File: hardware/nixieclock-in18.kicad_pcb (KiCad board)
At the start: 2 copper layers, 79 parts, among them J1 PROG, J2 POWER, Q1 BC848, Q10 MPSA42, Q11 MPSA42, Q12 MPSA42, Q13 MPSA42, Q14 MPSA42, Q15 MPSA42, Q16 MPSA42, Q17 MPSA42, Q18 MPSA42, Q19 MPSA42, Q2 BC858, Q20 MPSA42, Q21 MPSA42, Q3 Si4434, Q4 MPSA42, Q5 MPSA42, Q6 MPSA42, Q7 MPSA42, Q8 MPSA42, Q9 MPSA42, T1 IN18, T2 IN18, T3 IN18, T4 IN18, U1 LM1117-3.3, U2 DS3231M, U3 LM393, U4 ESP32-WROOM-32D

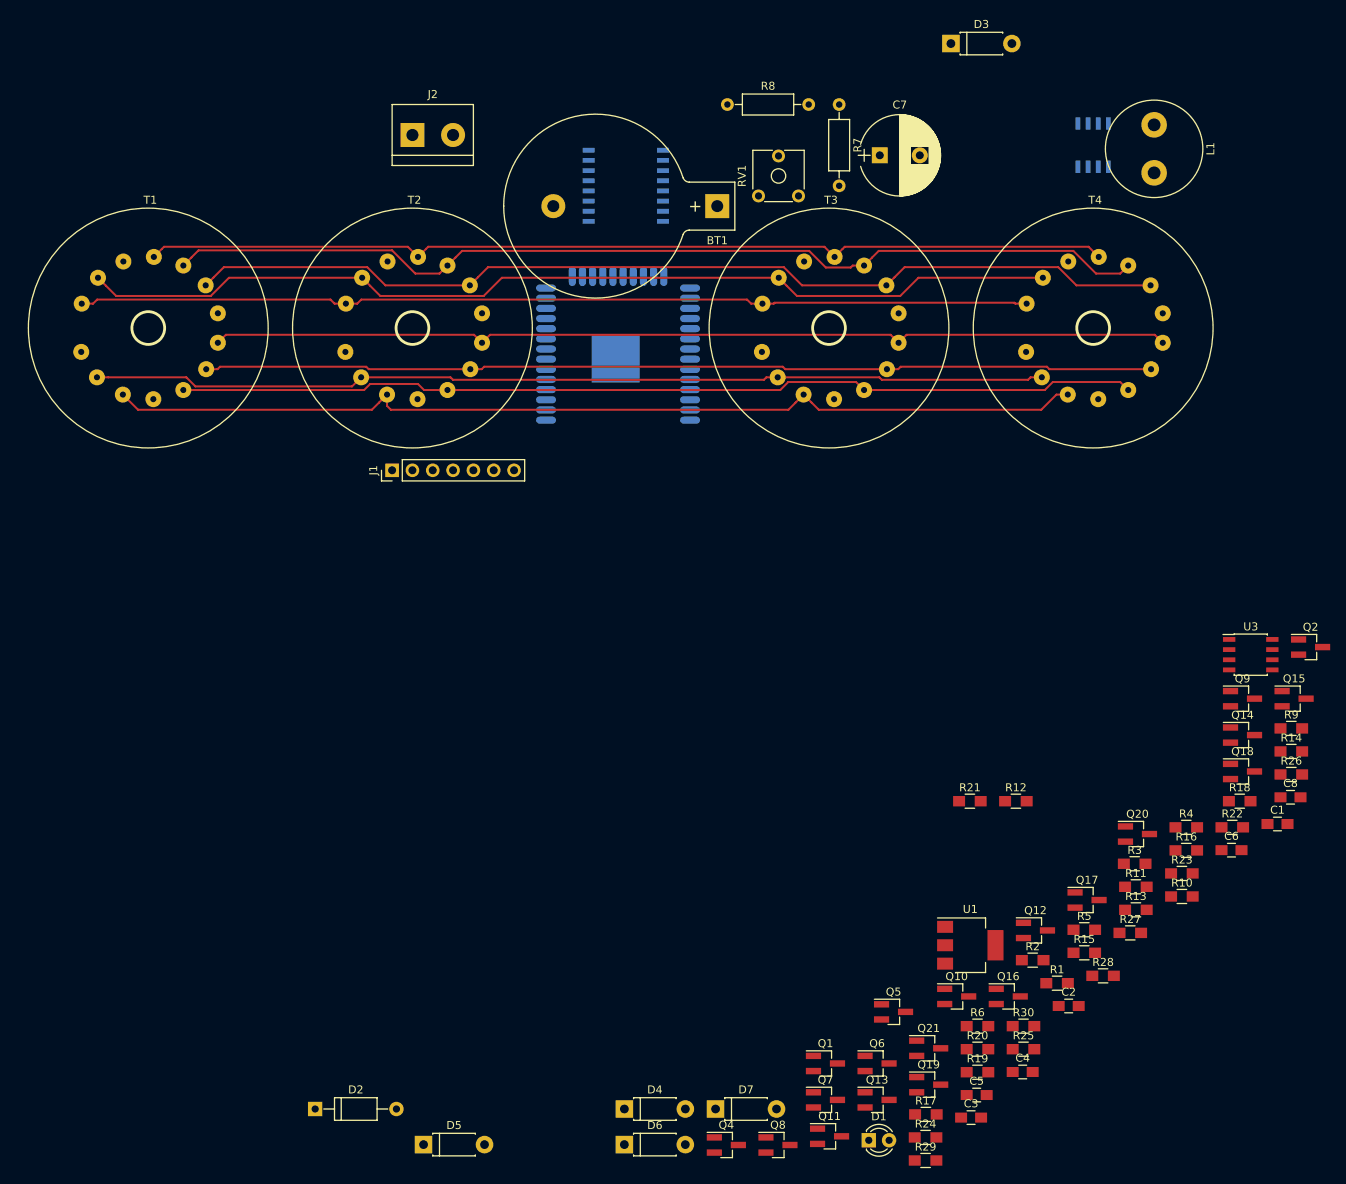
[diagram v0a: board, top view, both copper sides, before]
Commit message: fix mmbta42 pinout
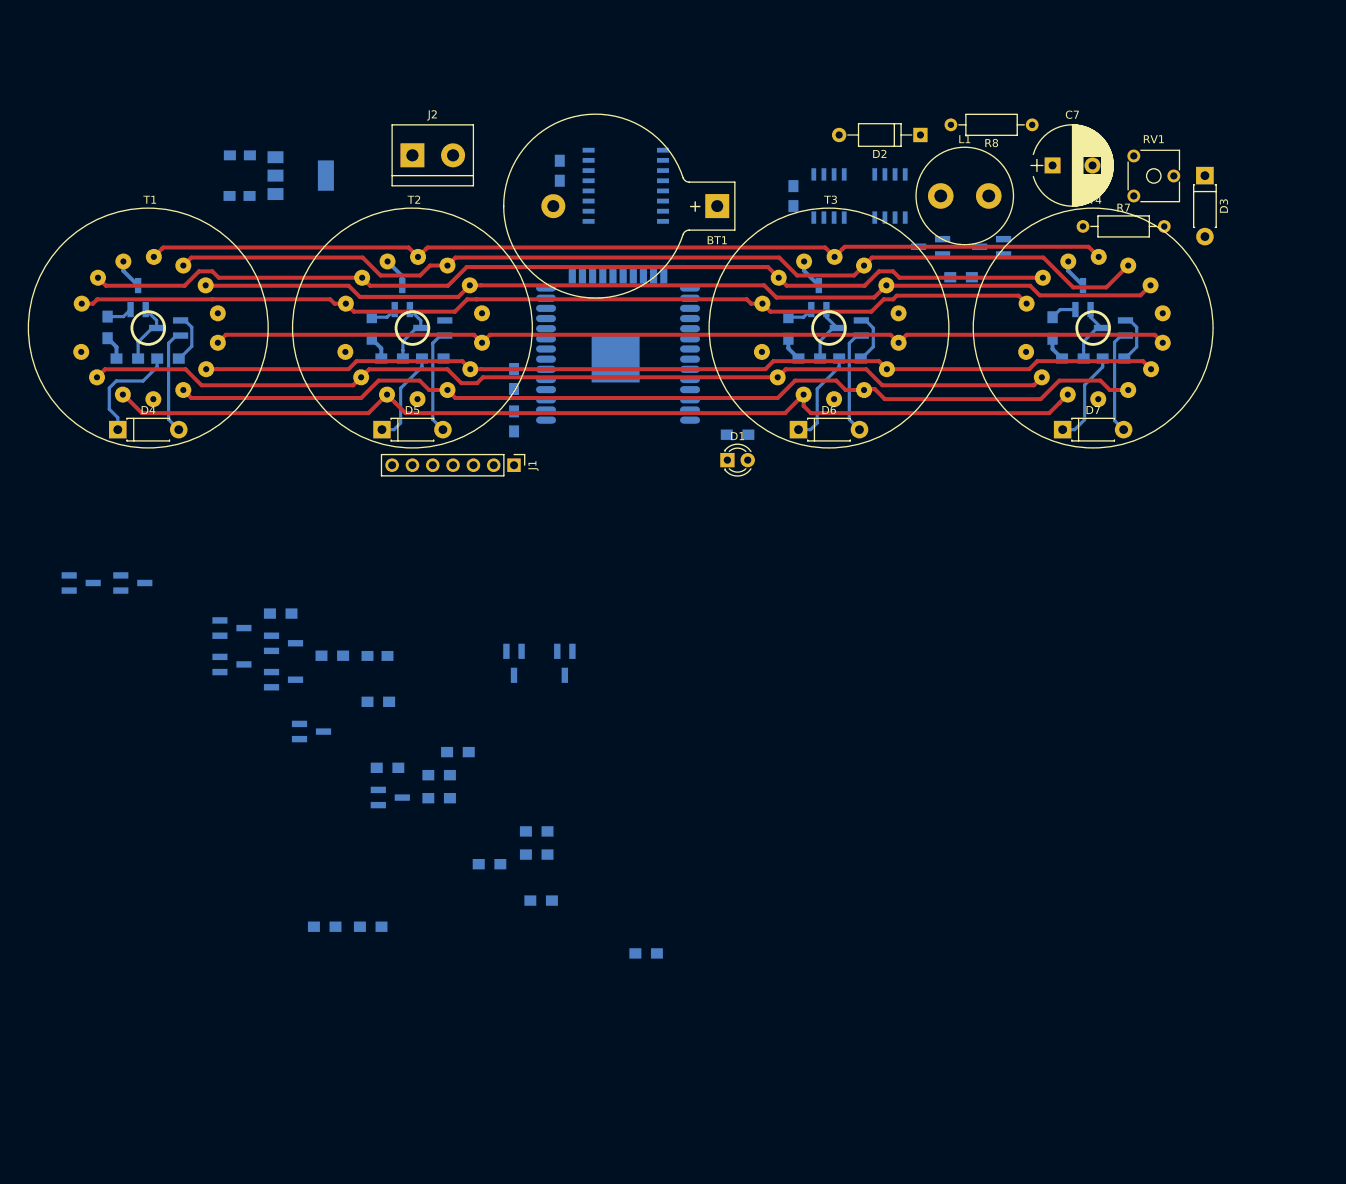
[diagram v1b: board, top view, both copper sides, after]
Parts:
- C1, C2, C3, C4, C5, C6, C8, Q1, Q2, R1, R10, R11, R12, R13, R14, R15, R16, R17, R18, R19, R2, R20, R21, R22, R23, R24, R25, R26, R27, R28, R29, R3, R30, R4, R5, R6, R9, U1, U3: moved to B.Cu
- Q10, Q11, Q12, Q13, Q14, Q15, Q16, Q17, Q18, Q19, Q20, Q21, Q4, Q5, Q6, Q7, Q8, Q9: value MPSA42 -> MMBTA42; moved to B.Cu
- moved C1 154.3 mm to (119.4, 57.1)
- moved R9 147.8 mm to (110.4, 82.5)
- moved R13 147.7 mm to (102.9, 78.7), turned to 270 degrees
- moved C3 147.1 mm to (119.4, 62.2), turned to 180 degrees
- moved D2 143.3 mm to (204.5, 54.6), turned to 180 degrees
- moved R11 142.3 mm to (105.3, 82.5), turned to 180 degrees
- moved Q7 132.1 mm to (106.7, 74.9), turned to 90 degrees
- moved U1 127.5 mm to (127.0, 59.7)
- moved Q5 124.6 mm to (110.5, 78.7), turned to 180 degrees
- moved R18 123.6 mm to (135.9, 78.7), turned to 270 degrees
- moved C2 122.3 mm to (159.4, 59.1), turned to 270 degrees
- moved R14 118.0 mm to (143.5, 82.5)
- moved Q11 117.7 mm to (139.7, 74.9), turned to 90 degrees
- moved R16 116.8 mm to (138.4, 82.5), turned to 180 degrees
- moved C5 114.7 mm to (188.6, 62.2), turned to 270 degrees
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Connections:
- Q10 pad 1: GND -> Net-(Q10-Pad1)
- Q10 pad 2: Net-(Q10-Pad2) -> GND
- Q11 pad 3: Net-(Q11-Pad3) -> /A1
- Q12 pad 1: GND -> Net-(Q12-Pad1)
- Q12 pad 2: Net-(Q12-Pad2) -> GND
- Q13 pad 1: GND -> Net-(Q13-Pad1)
- Q13 pad 2: Net-(Q13-Pad2) -> GND
- Q14 pad 1: GND -> Net-(Q14-Pad1)
- Q14 pad 2: Net-(Q14-Pad2) -> GND
- Q15 pad 1: GND -> Net-(Q15-Pad1)
- Q15 pad 2: Net-(Q15-Pad2) -> GND
- Q16 pad 1: Net-(Q16-Pad1) -> Net-(Q14-Pad3)
- Q16 pad 2: Net-(Q14-Pad3) -> Net-(Q16-Pad2)
- Q16 pad 3: Net-(Q16-Pad3) -> /A2
- Q17 pad 1: GND -> Net-(Q17-Pad1)
- Q17 pad 2: Net-(Q17-Pad2) -> GND
- Q18 pad 1: GND -> Net-(Q18-Pad1)
- Q18 pad 2: Net-(Q18-Pad2) -> GND
- Q19 pad 1: GND -> Net-(Q19-Pad1)
- Q19 pad 2: Net-(Q19-Pad2) -> GND
- Q20 pad 1: Net-(Q20-Pad1) -> Net-(Q18-Pad3)
- Q20 pad 2: Net-(Q18-Pad3) -> Net-(Q20-Pad2)
- Q20 pad 3: Net-(Q20-Pad3) -> /A3
- Q21 pad 1: GND -> Net-(Q21-Pad1)
- Q21 pad 2: Net-(Q21-Pad2) -> GND
- Q4 pad 1: GND -> Net-(Q4-Pad1)
- Q4 pad 2: Net-(Q4-Pad2) -> GND
- Q5 pad 1: GND -> Net-(Q5-Pad1)
- Q5 pad 2: Net-(Q5-Pad2) -> GND
- Q6 pad 1: GND -> Net-(Q6-Pad1)
- Q6 pad 2: Net-(Q6-Pad2) -> GND
- Q7 pad 1: Net-(Q7-Pad1) -> Net-(Q5-Pad3)
- Q7 pad 2: Net-(Q5-Pad3) -> Net-(Q7-Pad2)
- Q7 pad 3: Net-(Q7-Pad3) -> /A0
- Q8 pad 1: GND -> Net-(Q8-Pad1)
- Q8 pad 2: Net-(Q8-Pad2) -> GND
- Q9 pad 1: GND -> Net-(Q9-Pad1)
- Q9 pad 2: Net-(Q9-Pad2) -> GND
- Q9 pad 3: Net-(Q11-Pad2) -> Net-(Q11-Pad1)
- R1 pad 1: LED_SYNC -> (no net)
- R10 pad 1: DIG0 -> (no net)
- R10 pad 2: Net-(Q4-Pad2) -> Net-(Q4-Pad1)
- R12 pad 1: DIG1 -> (no net)
- R12 pad 2: Net-(Q6-Pad2) -> Net-(Q6-Pad1)
- R13 pad 1: Net-(Q7-Pad3) -> Net-(Q7-Pad2)
- R14 pad 2: Net-(Q9-Pad2) -> Net-(Q9-Pad1)
- R15 pad 1: DIG2 -> (no net)
- R15 pad 2: Net-(Q8-Pad2) -> Net-(Q8-Pad1)
- R16 pad 1: Net-(Q11-Pad2) -> Net-(Q11-Pad1)
- R17 pad 1: DIG3 -> (no net)
- R17 pad 2: Net-(Q10-Pad2) -> Net-(Q10-Pad1)
- R18 pad 1: Net-(Q11-Pad3) -> Net-(Q11-Pad2)
- R19 pad 1: DIG4 -> (no net)
- R19 pad 2: Net-(Q12-Pad2) -> Net-(Q12-Pad1)
- R20 pad 2: Net-(Q14-Pad2) -> Net-(Q14-Pad1)
- R21 pad 1: DIG5 -> (no net)
- R21 pad 2: Net-(Q13-Pad2) -> Net-(Q13-Pad1)
- R23 pad 1: DIG6 -> (no net)
- R23 pad 2: Net-(Q15-Pad2) -> Net-(Q15-Pad1)
- R24 pad 1: Net-(Q16-Pad3) -> Net-(Q16-Pad2)
- R25 pad 2: Net-(Q18-Pad2) -> Net-(Q18-Pad1)
- R26 pad 1: DIG7 -> (no net)
- R26 pad 2: Net-(Q17-Pad2) -> Net-(Q17-Pad1)
- R28 pad 1: DIG8 -> (no net)
- R28 pad 2: Net-(Q19-Pad2) -> Net-(Q19-Pad1)
- R29 pad 1: Net-(Q20-Pad3) -> Net-(Q20-Pad2)
- R30 pad 1: DIG9 -> (no net)
- R30 pad 2: Net-(Q21-Pad2) -> Net-(Q21-Pad1)
- R9 pad 2: Net-(Q5-Pad2) -> Net-(Q5-Pad1)
- T1 pad 1: Net-(T1-Pad1) -> (no net)
- T1 pad 12: Net-(Q7-Pad1) -> /A0
- T1 pad 4: Net-(Q7-Pad1) -> /A0
- T1 pad 8: Net-(T1-Pad8) -> (no net)
- T2 pad 1: Net-(T2-Pad1) -> (no net)
- T2 pad 12: Net-(Q11-Pad1) -> /A1
- T2 pad 4: Net-(Q11-Pad1) -> /A1
- T2 pad 8: Net-(T2-Pad8) -> (no net)
- T3 pad 1: Net-(T3-Pad1) -> (no net)
- T3 pad 12: Net-(Q16-Pad1) -> /A2
- T3 pad 4: Net-(Q16-Pad1) -> /A2
- T3 pad 8: Net-(T3-Pad8) -> (no net)
- T4 pad 1: Net-(T4-Pad1) -> (no net)
- T4 pad 12: Net-(Q20-Pad1) -> /A3
- T4 pad 4: Net-(Q20-Pad1) -> /A3
- T4 pad 8: Net-(T4-Pad8) -> (no net)
- U2 pad 1: Net-(U2-Pad1) -> (no net)
- U2 pad 3: Net-(U2-Pad3) -> (no net)
- U2 pad 4: Net-(U2-Pad4) -> (no net)
- U4 pad 10: Net-(U4-Pad10) -> (no net)
- U4 pad 13: Net-(U4-Pad13) -> (no net)
- U4 pad 14: Net-(U4-Pad14) -> (no net)
- U4 pad 16: Net-(U4-Pad16) -> (no net)
- U4 pad 17: Net-(U4-Pad17) -> (no net)
- U4 pad 18: Net-(U4-Pad18) -> (no net)
- U4 pad 19: Net-(U4-Pad19) -> (no net)
- U4 pad 20: Net-(U4-Pad20) -> (no net)
- U4 pad 21: Net-(U4-Pad21) -> (no net)
- U4 pad 22: Net-(U4-Pad22) -> (no net)
- U4 pad 23: Net-(U4-Pad23) -> (no net)
- U4 pad 24: Net-(U4-Pad24) -> (no net)
- U4 pad 26: Net-(U4-Pad26) -> (no net)
- U4 pad 27: Net-(U4-Pad27) -> (no net)
- U4 pad 28: Net-(U4-Pad28) -> (no net)
- U4 pad 29: Net-(U4-Pad29) -> (no net)
- U4 pad 31: Net-(U4-Pad31) -> (no net)
- U4 pad 32: Net-(U4-Pad32) -> (no net)
- U4 pad 33: Net-(U4-Pad33) -> (no net)
- U4 pad 36: Net-(U4-Pad36) -> (no net)
- U4 pad 37: Net-(U4-Pad37) -> (no net)
- U4 pad 4: Net-(U4-Pad4) -> (no net)
- U4 pad 5: Net-(U4-Pad5) -> (no net)
- U4 pad 7: Net-(U4-Pad7) -> (no net)
- U4 pad 8: Net-(U4-Pad8) -> (no net)
- U4 pad 9: Net-(U4-Pad9) -> (no net)
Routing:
- net GND: track 0.00 -> 52.8 mm
- net ~AN0: track 0.00 -> 13.8 mm
- net 170V: track 0.00 -> 11.9 mm
- net ~AN2: track 0.00 -> 11.9 mm
- net ~AN1: track 0.00 -> 11.8 mm
- net ~AN3: track 0.00 -> 11.8 mm
- net Net-(Q5-Pad3): track 0.00 -> 7.97 mm
- net Net-(Q18-Pad3): track 0.00 -> 7.93 mm
- net Net-(Q11-Pad1): track 0.00 -> 7.93 mm
- net Net-(Q14-Pad3): track 0.00 -> 7.90 mm
- net Net-(Q14-Pad1): track 0.00 -> 6.41 mm
- net Net-(Q5-Pad1): track 0.00 -> 6.40 mm
- net Net-(Q18-Pad1): track 0.00 -> 6.36 mm
- net /A0: track 0.00 -> 3.77 mm
- net /A3: track 0.00 -> 3.77 mm
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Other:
- net class Default: clearance 0.2 -> 0.25; trace_width 0.25 -> 0.4
- net class HV added: clearance 0.5, trace_width 0.5, via_dia 1, via_drill 0.6
- rule trace_clearance: 0.2 -> 0.25

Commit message: finished pcb
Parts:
- added F1: 100mA, Resistors_SMD:R_0805_HandSoldering, B.Cu at (114.3, 55.9)
- J1: footprint Pin_Headers:Pin_Header_Straight_1x07_Pitch2.54mm -> Pin_Headers:Pin_Header_Straight_1x06_Pitch2.54mm
- Q3: footprint Housings_SOIC:SOIC-8_3.9x4.9mm_Pitch1.27mm -> Housings_SOIC:PowerPAK_SO-8_Single
- moved R3 95.0 mm to (188.0, 58.4), turned to 180 degrees
- moved R12 94.3 mm to (179.1, 69.8), turned to 90 degrees
- moved R4 92.2 mm to (184.2, 62.2), turned to 270 degrees
- moved Q12 91.6 mm to (213.4, 85.1), turned to 270 degrees
- moved R19 90.3 mm to (212.0, 80.0)
- moved R2 84.2 mm to (187.9, 66.0), turned to 180 degrees
- moved Q6 84.0 mm to (184.2, 68.6)
- moved R15 78.8 mm to (113.1, 62.2), turned to 180 degrees
- moved R10 78.8 mm to (127.0, 68.6), turned to 270 degrees
- moved R26 74.5 mm to (203.2, 90.2)
- moved Q21 72.4 mm to (180.3, 76.2), turned to 90 degrees
- moved R28 72.3 mm to (119.4, 64.8), turned to 180 degrees
- moved R23 71.0 mm to (124.5, 81.2), turned to 270 degrees
- moved R21 66.1 mm to (125.7, 87.6), turned to 270 degrees
- moved R30 62.1 mm to (180.3, 81.3)
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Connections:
- J2 pad 1: +15V -> Net-(F1-Pad1)
- R1 pad 1: (no net) -> LED_SYNC
- R10 pad 1: (no net) -> DIG0
- R12 pad 1: (no net) -> DIG1
- R15 pad 1: (no net) -> DIG2
- R17 pad 1: (no net) -> DIG3
- R19 pad 1: (no net) -> DIG4
- R21 pad 1: (no net) -> DIG5
- R23 pad 1: (no net) -> DIG6
- R26 pad 1: (no net) -> DIG7
- R28 pad 1: (no net) -> DIG8
- R30 pad 1: (no net) -> DIG9
- U4 pad 17: (no net) -> DIG5
- U4 pad 18: (no net) -> DIG6
- U4 pad 19: (no net) -> DIG3
- U4 pad 21: (no net) -> DIG0
- U4 pad 22: (no net) -> DIG8
- U4 pad 23: (no net) -> DIG2
- U4 pad 26: (no net) -> DIG1
- U4 pad 27: (no net) -> DIG4
- U4 pad 28: (no net) -> DIG7
- U4 pad 31: (no net) -> DIG9
- U4 pad 33: (no net) -> ~AN3
- U4 pad 36: (no net) -> ~AN2
- U4 pad 37: (no net) -> LED_SYNC
- U4 pad 7: (no net) -> ~AN1
- U4 pad 8: (no net) -> ~AN0
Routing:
- net GND: track 52.8 -> 658.8 mm, vias 0 -> 11
- net 170V: track 11.9 -> 190.1 mm, vias 0 -> 4
- net +3V3: track 0.00 -> 172.6 mm, vias 0 -> 1
- net FB: track 0.00 -> 130.0 mm, vias 0 -> 1
- net +15V: track 0.00 -> 122.6 mm, vias 0 -> 1
- net DIG4: track 0.00 -> 87.6 mm, vias 0 -> 4
- net DIG2: track 0.00 -> 78.7 mm, vias 0 -> 4
- net IO0: track 0.00 -> 75.4 mm, vias 0 -> 2
- net ~AN0: track 13.8 -> 89.0 mm, vias 0 -> 4
- net DIG8: track 0.00 -> 72.2 mm, vias 0 -> 4
- net DIG5: track 0.00 -> 71.4 mm, vias 0 -> 4
- net DIG6: track 0.00 -> 68.9 mm, vias 0 -> 4
- net DIG3: track 0.00 -> 67.2 mm, vias 0 -> 6
- net DIG0: track 0.00 -> 65.8 mm, vias 0 -> 4
- net DIG7: track 0.00 -> 63.0 mm, vias 0 -> 4
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- added copper zone on B.Cu, net GND
- added copper zone on F.Cu, net GND
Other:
- board outline added: 151.1 x 47 mm

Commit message: gerbers
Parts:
- added REF**: MountingHole_3.2mm_M3, Mounting_Holes:MountingHole_3.2mm_M3, F.Cu at (95.2, 94.0)
- added REF**: MountingHole_3.2mm_M3, Mounting_Holes:MountingHole_3.2mm_M3, F.Cu at (238.8, 94.0)
- added REF**: MountingHole_3.2mm_M3, Mounting_Holes:MountingHole_3.2mm_M3, F.Cu at (238.8, 54.6)
- added REF**: MountingHole_3.2mm_M3, Mounting_Holes:MountingHole_3.2mm_M3, F.Cu at (95.2, 54.6)
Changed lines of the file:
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@@
     (tracks 979)
     (zones 0)
-    (modules 80)
+    (modules 84)
     (nets 73)
   )
@@
     (visible_elements FFFFFF7F)
     (pcbplotparams
-      (layerselection 0x010fc_ffffffff)
-      (usegerberextensions false)
+      (layerselection 0x010f0_ffffffff)
+      (usegerberextensions true)
       (usegerberattributes false)
       (usegerberadvancedattributes false)
@@
       (outputformat 1)
       (mirror false)
-      (drillshape 1)
+      (drillshape 0)
       (scaleselection 1)
-      (outputdirectory ""))
+      (outputdirectory "gerbers/"))
   )
   (net 0 "")
@@
     (add_net "Net-(R7-Pad2)")
     (add_net "Net-(R8-Pad1)")
-    (add_net "Net-(T1-Pad1)")
-    (add_net "Net-(T1-Pad8)")
-    (add_net "Net-(T2-Pad1)")
-    (add_net "Net-(T2-Pad8)")
-    (add_net "Net-(T3-Pad1)")
-    (add_net "Net-(T3-Pad8)")
-    (add_net "Net-(T4-Pad1)")
-    (add_net "Net-(T4-Pad8)")
-    (add_net "Net-(U2-Pad1)")
-    (add_net "Net-(U2-Pad3)")
-    (add_net "Net-(U2-Pad4)")
-    (add_net "Net-(U4-Pad10)")
-    (add_net "Net-(U4-Pad13)")
-    (add_net "Net-(U4-Pad14)")
-    (add_net "Net-(U4-Pad16)")
-    (add_net "Net-(U4-Pad20)")
-    (add_net "Net-(U4-Pad24)")
-    (add_net "Net-(U4-Pad29)")
-    (add_net "Net-(U4-Pad32)")
-    (add_net "Net-(U4-Pad4)")
-    (add_net "Net-(U4-Pad5)")
-    (add_net "Net-(U4-Pad9)")
     (add_net PWM)
     (add_net UART_RX)
@@
     (add_net 170V)
   )
+  (module Mounting_Holes:MountingHole_3.2mm_M3 (layer F.Cu)
+    (at 95.25 93.98)
+    (descr "Mounting Hole 3.2mm, no annular, M3")
+    (tags "mounting hole 3.2mm no annular m3")
+    (attr virtual)
+    (fp_text reference REF** (at 0 -4.2) (layer F.SilkS) hide
+      (effects (font (size 1 1) (thickness 0.15)))
+    )
+    (fp_text value MountingHole_3.2mm_M3 (at 0 4.2) (layer F.Fab)
+      (effects (font (size 1 1) (thickness 0.15)))
+    )
+    (fp_circle (center 0 0) (end 3.45 0) (layer F.CrtYd) (width 0.05))
+    (fp_circle (center 0 0) (end 3.2 0) (layer Cmts.User) (width 0.15))
+    (fp_text user %R (at 0.3 0) (layer F.Fab)
+      (effects (font (size 1 1) (thickness 0.15)))
+    )
+    (pad 1 np_thru_hole circle (at 0 0) (size 3.2 3.2) (drill 3.2) (layers *.Cu *.Mask))
+  )
+  (module Mounting_Holes:MountingHole_3.2mm_M3 (layer F.Cu)
+    (at 238.76 93.98)
+    (descr "Mounting Hole 3.2mm, no annular, M3")
+    (tags "mounting hole 3.2mm no annular m3")
+    (attr virtual)
+    (fp_text reference REF** (at 0 -4.2) (layer F.SilkS) hide
+      (effects (font (size 1 1) (thickness 0.15)))
+    )
+    (fp_text value MountingHole_3.2mm_M3 (at 0 4.2) (layer F.Fab)
+      (effects (font (size 1 1) (thickness 0.15)))
+    )
+    (fp_text user %R (at 0.3 0) (layer F.Fab)
+      (effects (font (size 1 1) (thickness 0.15)))
+    )
+    (fp_circle (center 0 0) (end 3.2 0) (layer Cmts.User) (width 0.15))
+    (fp_circle (center 0 0) (end 3.45 0) (layer F.CrtYd) (width 0.05))
+    (pad 1 np_thru_hole circle (at 0 0) (size 3.2 3.2) (drill 3.2) (layers *.Cu *.Mask))
+  )
+  (module Mounting_Holes:MountingHole_3.2mm_M3 (layer F.Cu)
+    (at 238.76 54.61)
+    (descr "Mounting Hole 3.2mm, no annular, M3")
+    (tags "mounting hole 3.2mm no annular m3")
+    (attr virtual)
+    (fp_text reference REF** (at 0 -4.2) (layer F.SilkS) hide
+      (effects (font (size 1 1) (thickness 0.15)))
+    )
+    (fp_text value MountingHole_3.2mm_M3 (at 0 4.2) (layer F.Fab)
+      (effects (font (size 1 1) (thickness 0.15)))
+    )
+    (fp_circle (center 0 0) (end 3.45 0) (layer F.CrtYd) (width 0.05))
+    (fp_circle (center 0 0) (end 3.2 0) (layer Cmts.User) (width 0.15))
+    (fp_text user %R (at 0.3 0) (layer F.Fab)
+      (effects (font (size 1 1) (thickness 0.15)))
+    )
+    (pad 1 np_thru_hole circle (at 0 0) (size 3.2 3.2) (drill 3.2) (layers *.Cu *.Mask))
+  )
+  (module Mounting_Holes:MountingHole_3.2mm_M3 (layer F.Cu)
+    (at 95.25 54.61)
+    (descr "Mounting Hole 3.2mm, no annular, M3")
+    (tags "mounting hole 3.2mm no annular m3")
+    (attr virtual)
+    (fp_text reference REF** (at 0 -4.2) (layer F.SilkS) hide
+      (effects (font (size 1 1) (thickness 0.15)))
+    )
+    (fp_text value MountingHole_3.2mm_M3 (at 0 4.2) (layer F.Fab)
+      (effects (font (size 1 1) (thickness 0.15)))
+    )
+    (fp_text user %R (at 0.3 0) (layer F.Fab)
+      (effects (font (size 1 1) (thickness 0.15)))
+    )
+    (fp_circle (center 0 0) (end 3.2 0) (layer Cmts.User) (width 0.15))
+    (fp_circle (center 0 0) (end 3.45 0) (layer F.CrtYd) (width 0.05))
+    (pad 1 np_thru_hole circle (at 0 0) (size 3.2 3.2) (drill 3.2) (layers *.Cu *.Mask))
+  )
   (module Resistors_SMD:R_0805_HandSoldering (layer B.Cu)
     (at 114.3 55.88 270)
@@
     (connect_pads (clearance 0.508))
     (min_thickness 0.254)
-    (fill (arc_segments 32) (thermal_gap 0.508) (thermal_bridge_width 0.508))
+    (fill yes (arc_segments 32) (thermal_gap 0.508) (thermal_bridge_width 0.508))
     (polygon
       (pts
@@
     (connect_pads (clearance 0.508))
     (min_thickness 0.254)
-    (fill (arc_segments 32) (thermal_gap 0.508) (thermal_bridge_width 0.508))
+    (fill yes (arc_segments 32) (thermal_gap 0.508) (thermal_bridge_width 0.508))
     (polygon
       (pts
